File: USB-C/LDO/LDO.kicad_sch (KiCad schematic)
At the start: 32 parts, among them J1 USB_C_Receptacle_PowerOnly_6P, J2 Conn_01x03_Pin, J3 AudioJack2_Ground, J4 AudioJack2_Ground, J5 Conn_02x04_Odd_Even, J6 Conn_02x04_Odd_Even, U1 LM27762, U2 OPA1655

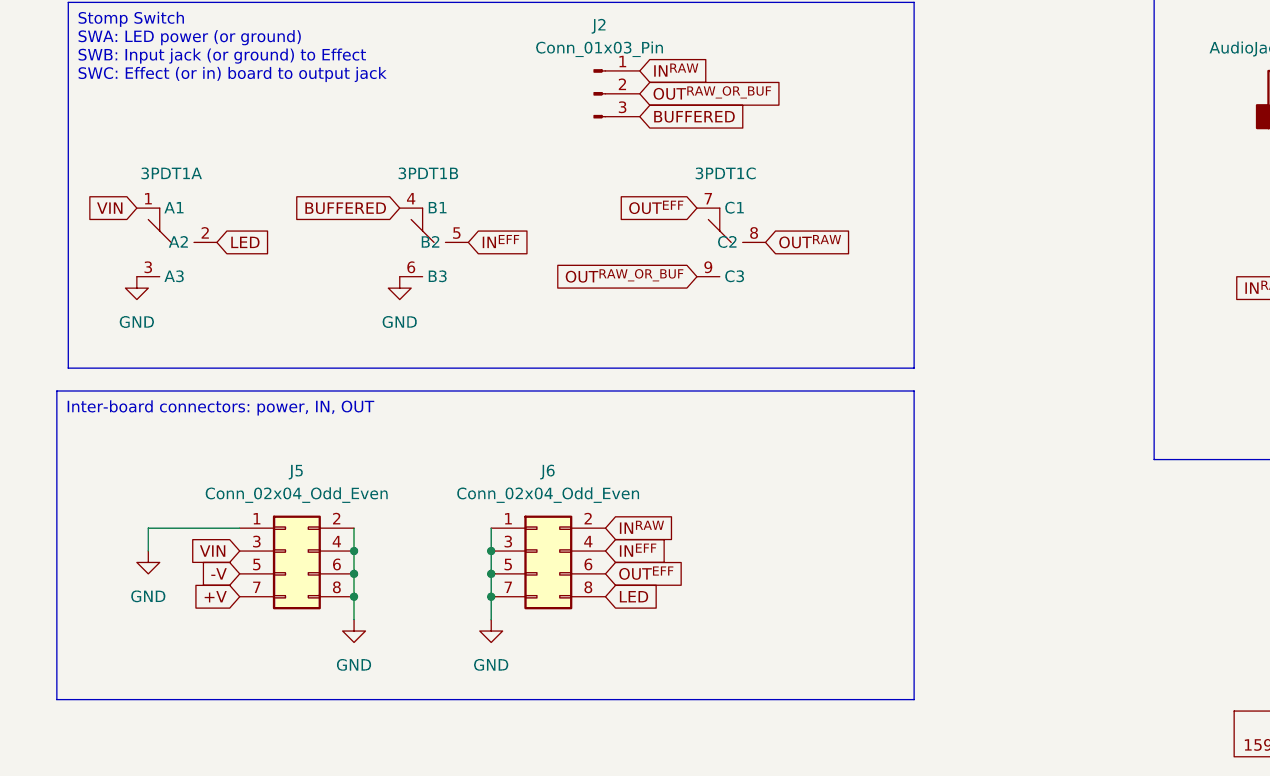
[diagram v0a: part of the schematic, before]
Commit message: Convert the USB LDO base board and the Octaver to 2-layer boards
I said I wouldn't do this, because 4-layer boards just makes it easier
being lazy, and doesn't involve messing up the gerbers by switching
stack-up in the middle of the project.

But I wanted to see how painful it would be, particularly with the
fairly packed Octaver board (well, packed for _me_, not like it's
actually all that full).

The inner layers were pretty empty anyway, since I tend to try to avoid
via routing and mainly used them for some power routing, and it really
wasn't that much work.

I've switched to the new smaller Murata caps on these boards at the same
time.

Signed-off-by: Linus Torvalds <torvalds@linux-foundation.org>
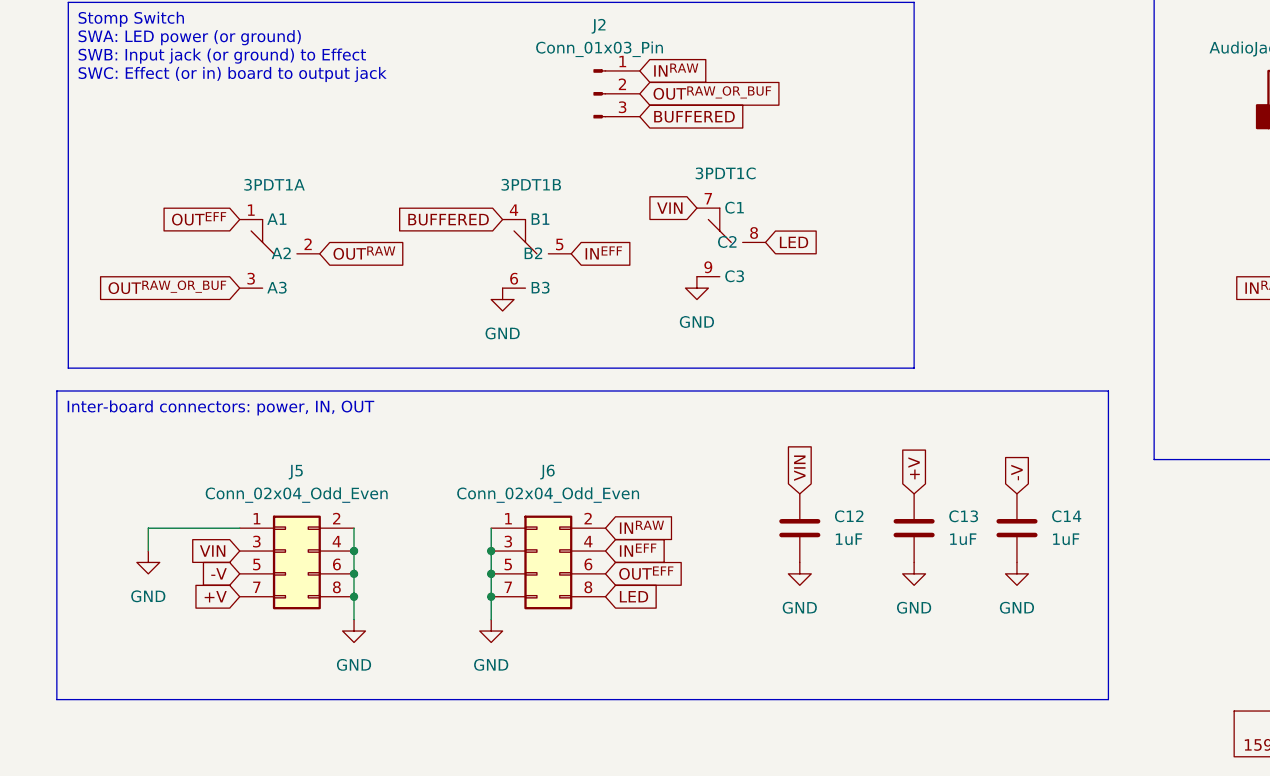
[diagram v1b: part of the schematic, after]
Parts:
- added C12, C13, C14: 1uF, Capacitor_SMD:C_1206_3216Metric_Pad1.33x1.80mm_HandSolder, symbol Device:C
- C10, C11, C9: footprint Capacitor_SMD:C_1206_3216Metric_Pad1.33x1.80mm_HandSolder -> Mylib:C_0704_1810Metric
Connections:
- net +V: now also C13.1
- net -V: now also C14.1
- net GND: now also 3PDT1.9 (C3), C12.2, C13.2, C14.2; no longer 3PDT1.3 (A3)
- net LED: now also 3PDT1.8 (C2); no longer 3PDT1.2 (A2)
- net OUT^{EFF}: now also 3PDT1.1 (A1); no longer 3PDT1.7 (C1)
- net OUT^{RAW_OR_BUF}: now also 3PDT1.3 (A3); no longer 3PDT1.9 (C3)
- net OUT^{RAW}: now also 3PDT1.2 (A2); no longer 3PDT1.8 (C2)
- net VIN: now also 3PDT1.7 (C1), C12.1; no longer 3PDT1.1 (A1)
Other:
- moved on the sheet: 3PDT1A, 3PDT1B

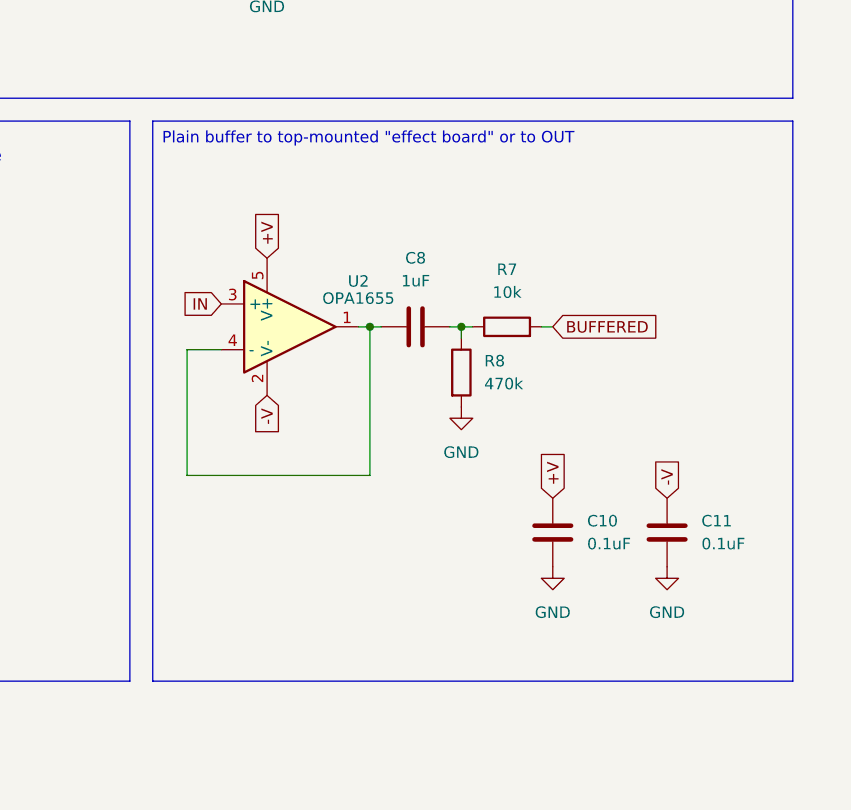
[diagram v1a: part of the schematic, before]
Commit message: Allow trimming gain on base board input buffer
Instead of just having a unity gain buffer, let's add a trim pot that
allows for higher input gain when that makes sense for the effect board.

For example, the very traditional Big Muff fuzz pedal seems to have an
input stage with roughly a voltage gain of 7x (+17dB).

Random pick: 100k trim pot with 10k resistor gives a gain range of 1-11.

Signed-off-by: Linus Torvalds <torvalds@linux-foundation.org>
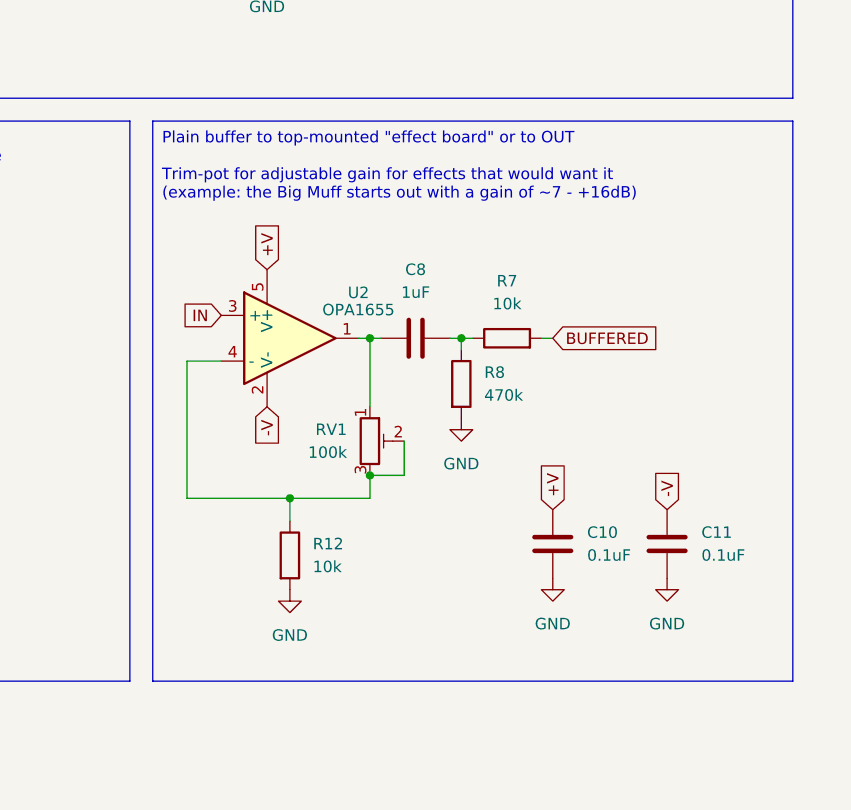
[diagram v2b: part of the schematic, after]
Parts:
- added R12: 10k, Resistor_SMD:R_0805_2012Metric_Pad1.20x1.40mm_HandSolder, symbol Device:R
- added RV1: 100k, Mylib:Bourns_3362S, symbol Device:R_Potentiometer_Trim
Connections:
- net GND: now also R12.2
- net at C8.1, U2.1: now also RV1.1; no longer U2.4 (-)
- new net: R12.1, RV1.2, RV1.3, U2.4 (-)
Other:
- moved on the sheet: C10, C11, C8, R7, R8, U2
